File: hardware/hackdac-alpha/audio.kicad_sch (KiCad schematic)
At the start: 30 parts, among them J3 I2C, J4 AUDIO OUT, P2 P22, Q4 2N7002, Q5 2N7002, U8 MCP1700T-3302E/MB, U9 PCM5102

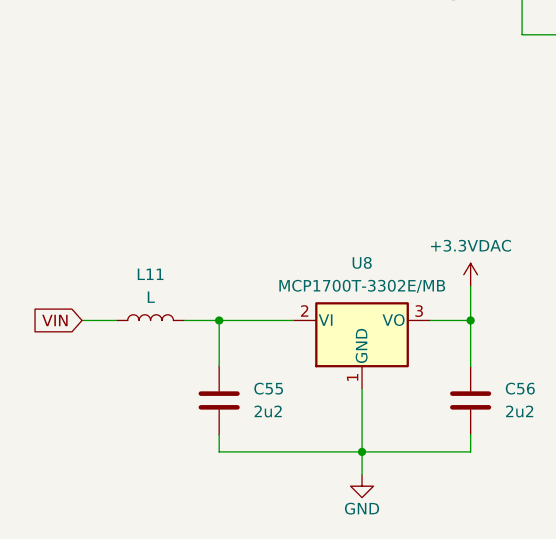
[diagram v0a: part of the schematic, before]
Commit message: Add missing component values
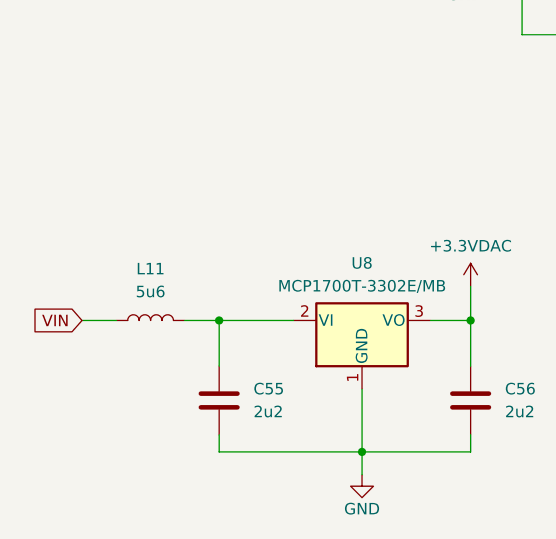
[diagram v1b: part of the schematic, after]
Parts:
- L11: value L -> 5u6
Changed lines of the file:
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@@
 		(fields_autoplaced yes)
 		(property "Reference" "L11"
-			(at 48.895 151.765 90)
+			(at 48.895 151.13 90)
 			(effects
 				(font
@@
 			)
 		)
-		(property "Value" "L"
-			(at 48.895 154.305 90)
+		(property "Value" "5u6"
+			(at 48.895 153.67 90)
 			(effects
 				(font

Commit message: Update with V2 mods
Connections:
- net TCXO_CLK: now reaches P2.2 (Pin_2)
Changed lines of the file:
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@@
+	(wire
+		(pts
+			(xy 76.2 29.845) (xy 80.01 29.845)
+		)
+		(stroke
+			(width 0)
+			(type default)
+		)
+	)
 	(wire
 		(pts
@@
 				(hide yes)
 			)
+		)
+	)
+	(global_label "TCXO_CLK"
+		(shape input)
+		(at 80.01 29.845 0)
+		(fields_autoplaced yes)
+		(effects
+			(font
+				(size 1.27 1.27)
+			)
+			(justify left)
+		)
+		(property "Intersheetrefs" "${INTERSHEET_REFS}"
+			(at 92.3085 29.845 0)
+			(effects
+				(font
+					(size 1.27 1.27)
+				)
+				(justify left)
+				(hide yes)
+			)

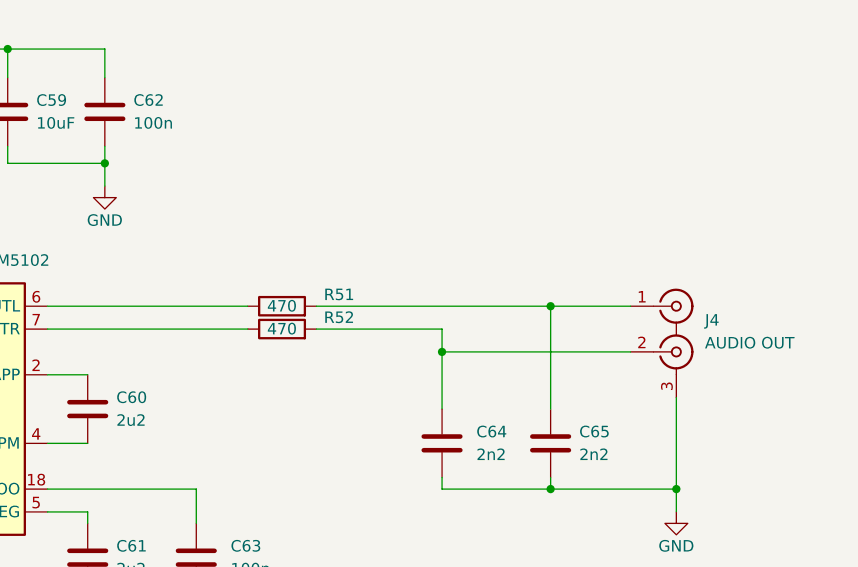
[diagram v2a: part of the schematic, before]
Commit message: Final values for V2 board
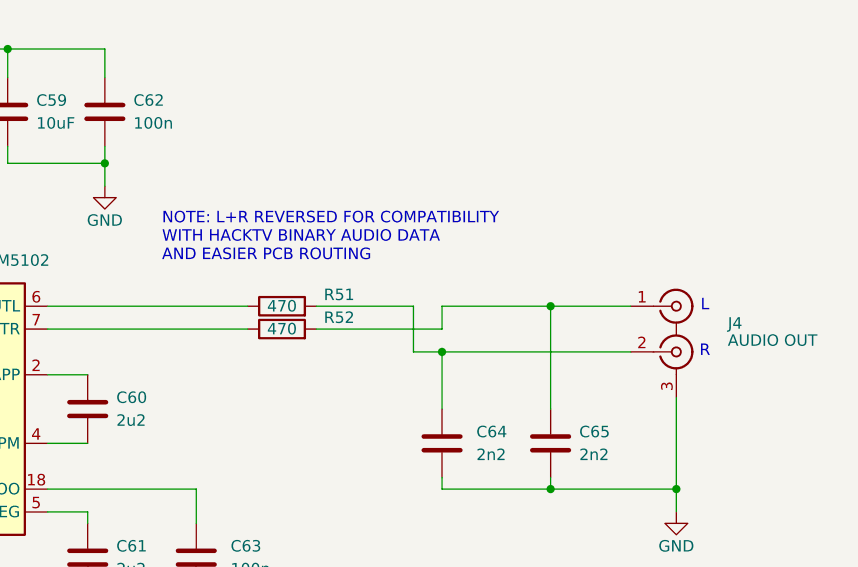
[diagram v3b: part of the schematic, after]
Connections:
- net at C64.1, J4.2 (IN2): now also R51.2; no longer R52.2
- net at C65.1, J4.1 (IN1): now also R52.2; no longer R51.2
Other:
- note added: "L"
- note added: "NOTE: L+R REVERSED FOR COMPATIBILITY WITH HACKTV BINARY AUDIO DATA AND EASIER PCB ROUTING"
- note added: "R"
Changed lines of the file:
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@@
 	)
 	(junction
+		(at 224.79 114.935)
+		(diameter 0)
+		(color 0 0 0 0)
+	)
+	(junction
 		(at 236.855 109.855)
 		(diameter 0)
@@
 		(color 0 0 0 0)
 	)
-	(junction
-		(at 224.79 114.935)
-		(diameter 0)
-		(color 0 0 0 0)
-	)
 	(wire
 		(pts
@@
 	(wire
 		(pts
+			(xy 221.615 114.935) (xy 224.79 114.935)
+		)
+		(stroke
+			(width 0)
+			(type default)
+		)
+	)
+	(wire
+		(pts
+			(xy 221.615 109.855) (xy 221.615 114.935)
+		)
+		(stroke
+			(width 0)
+			(type default)
+		)
+	)
+	(wire
+		(pts
 			(xy 185.42 141.605) (xy 185.42 142.875)
 		)
@@
 	(wire
 		(pts
+			(xy 210.82 109.855) (xy 221.615 109.855)
+		)
+		(stroke
+			(width 0)
+			(type default)
+		)
+	)
+	(wire
+		(pts
 			(xy 153.67 117.475) (xy 155.575 117.475)
 		)
@@
 	(wire
 		(pts
+			(xy 224.79 109.855) (xy 236.855 109.855)
+		)
+		(stroke
+			(width 0)
+			(type default)
+		)
+	)
+	(wire
+		(pts
 			(xy 147.955 127.635) (xy 155.575 127.635)
 		)
@@
 	(wire
 		(pts
-			(xy 197.485 130.175) (xy 197.485 133.985)
+			(xy 224.79 112.395) (xy 224.79 109.855)
 		)
 		(stroke
@@
 	(wire
 		(pts
-			(xy 84.455 156.845) (xy 84.455 161.925)
+			(xy 197.485 130.175) (xy 197.485 133.985)
 		)
 		(stroke
@@
 	(wire
 		(pts
-			(xy 176.53 81.28) (xy 176.53 84.455)
+			(xy 84.455 156.845) (xy 84.455 161.925)
 		)
 		(stroke
@@
 	(wire
 		(pts
-			(xy 210.82 112.395) (xy 224.79 112.395)
+			(xy 176.53 81.28) (xy 176.53 84.455)
 		)
 		(stroke
@@
 	(wire
 		(pts
-			(xy 139.7 117.475) (xy 144.145 117.475)
+			(xy 210.82 112.395) (xy 224.79 112.395)
 		)
 		(stroke
@@
 	(wire
 		(pts
-			(xy 224.79 130.175) (xy 224.79 128.905)
+			(xy 139.7 117.475) (xy 144.145 117.475)
 		)
 		(stroke
@@
 	(wire
 		(pts
-			(xy 130.175 49.53) (xy 130.175 34.29)
+			(xy 224.79 130.175) (xy 224.79 128.905)
 		)
 		(stroke
@@
 	(wire
 		(pts
-			(xy 168.275 137.795) (xy 168.275 140.335)
+			(xy 130.175 49.53) (xy 130.175 34.29)
 		)
 		(stroke
@@
 	(wire
 		(pts
-			(xy 224.79 112.395) (xy 224.79 114.935)
+			(xy 168.275 137.795) (xy 168.275 140.335)
 		)
 		(stroke
@@
 	(wire
 		(pts
-			(xy 210.82 109.855) (xy 236.855 109.855)
-		)
-		(stroke
-			(width 0)
-			(type default)
-		)
-	)
-	(wire
-		(pts
 			(xy 180.975 117.475) (xy 185.42 117.475)
 		)
@@
 		)
 	)
+	(text "NOTE: L+R REVERSED FOR COMPATIBILITY\nWITH HACKTV BINARY AUDIO DATA\nAND EASIER PCB ROUTING"
+		(exclude_from_sim no)
+		(at 193.675 102.235 0)
+		(effects
+			(font
+				(size 1.27 1.27)
+			)
+			(justify left)
+		)
+	)
+	(text "R"
+		(exclude_from_sim no)
+		(at 254 114.935 0)
+		(effects
+			(font
+				(size 1.27 1.27)
+			)
+		)
+	)
+	(text "L"
+		(exclude_from_sim no)
+		(at 254 109.855 0)
+		(effects
+			(font
+				(size 1.27 1.27)
+			)
+		)
+	)
 	(label "I2S_WS"
 		(at 50.165 47.625 0)
@@
 		(on_board yes)
 		(dnp no)
-		(fields_autoplaced yes)
 		(property "Reference" "J4"
-			(at 254 111.4182 0)
+			(at 256.54 111.76 0)
 			(effects
 				(font
@@
 		)
 		(property "Value" "AUDIO OUT"
-			(at 254 113.9582 0)
+			(at 256.54 113.665 0)
 			(effects
 				(font

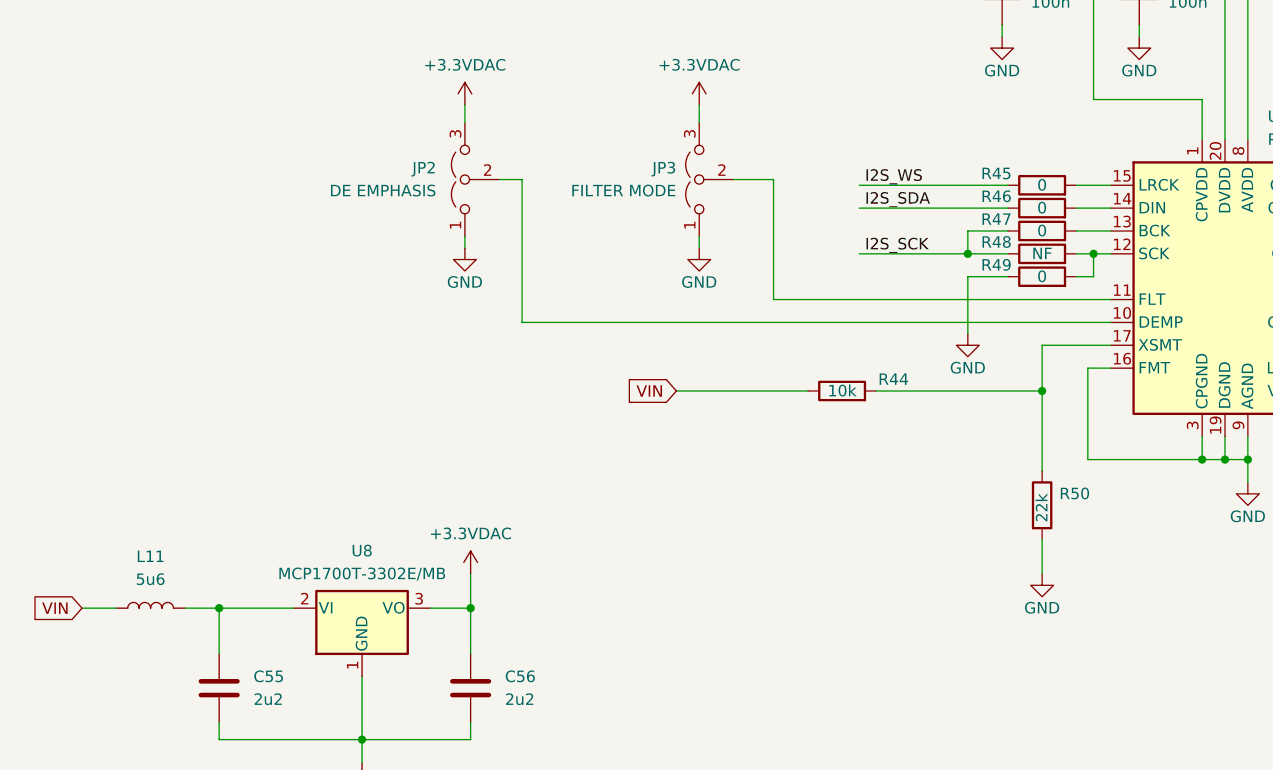
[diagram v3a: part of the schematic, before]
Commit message: More V3 component rationalisation
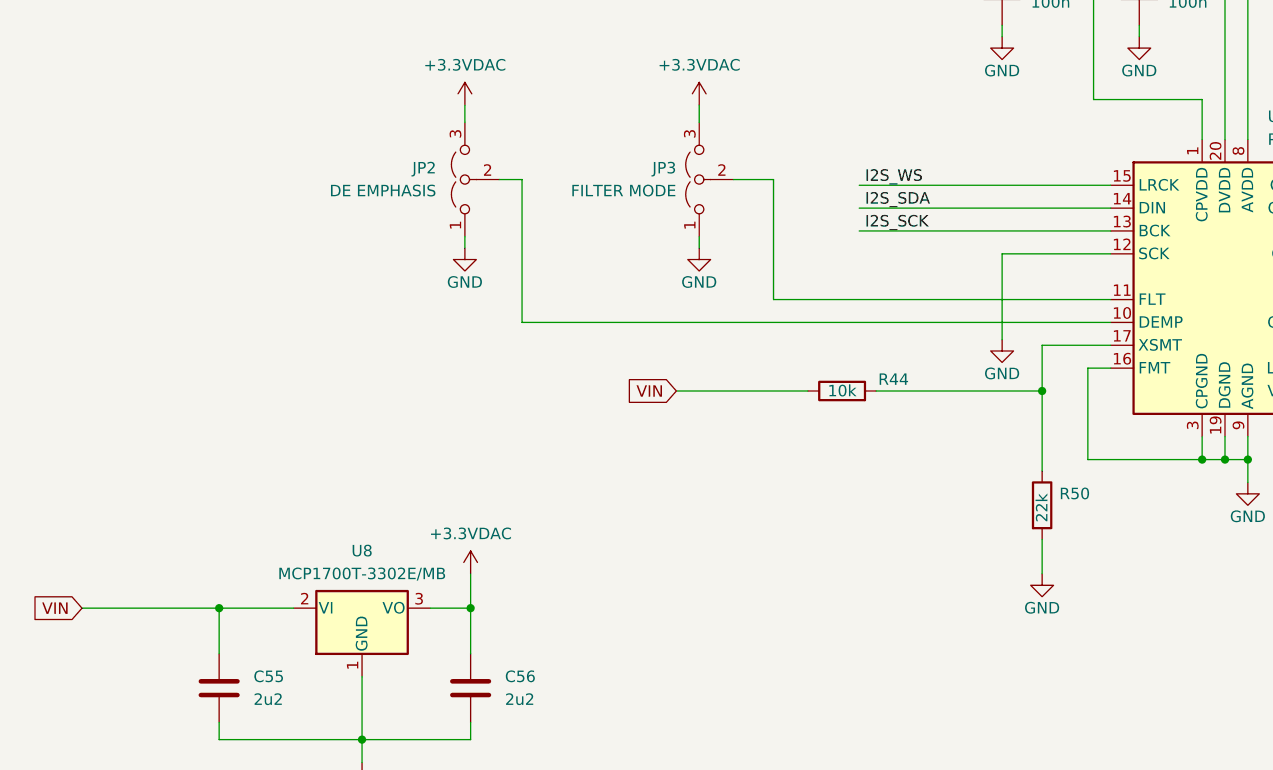
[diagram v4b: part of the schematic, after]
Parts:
- removed L11: 5u6, Inductor_SMD:L_1210_3225Metric, symbol Device:L
- removed R45, R46, R47, R49: 0, Resistor_SMD:R_0603_1608Metric, symbol Device:R
- removed R48: NF, Resistor_SMD:R_0603_1608Metric, symbol Device:R
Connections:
- net GND: now also U9.12 (SCK)
- net I2S_SCK: now also U9.13 (BCK)
- net I2S_SDA: now also U9.14 (DIN)
- net I2S_WS: now also U9.15 (LRCK)
- net VIN: now also C55.1, U8.2 (VI)

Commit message: Last of major V3 changes
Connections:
- net PWR_EN: now reaches P2.22 (Pin_22)
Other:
- note added: "NO FIT"
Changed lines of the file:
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@@
+	(wire
+		(pts
+			(xy 76.2 55.245) (xy 81.915 55.245)
+		)
+		(stroke
+			(width 0)
+			(type default)
+		)
+	)
 	(wire
 		(pts
@@
 	(wire
 		(pts
-			(xy 97.155 57.785) (xy 97.155 49.53)
+			(xy 98.425 57.785) (xy 98.425 49.53)
 		)
 		(stroke
@@
 	(wire
 		(pts
-			(xy 76.2 57.785) (xy 97.155 57.785)
+			(xy 76.2 57.785) (xy 98.425 57.785)
 		)
 		(stroke
@@
 	(wire
 		(pts
-			(xy 97.155 49.53) (xy 100.33 49.53)
+			(xy 98.425 49.53) (xy 100.33 49.53)
 		)
 		(stroke
@@
 	(text "NOTE: L+R REVERSED FOR COMPATIBILITY\nWITH HACKTV BINARY AUDIO DATA\nAND EASIER PCB ROUTING"
 		(exclude_from_sim no)
-		(at 193.675 102.235 0)
+		(at 204.47 102.235 0)
 		(effects
 			(font
@@
 			)
 			(justify left)
+		)
+	)
+	(text "NO FIT"
+		(exclude_from_sim no)
+		(at 147.32 38.1 0)
+		(effects
+			(font
+				(size 1.27 1.27)
+			)
 		)
 	)
@@
 	)
 	(label "SCL"
-		(at 82.55 60.325 0)
+		(at 93.345 60.325 0)
 		(fields_autoplaced yes)
 		(effects
@@
 	)
 	(label "SDA"
-		(at 82.55 57.785 0)
+		(at 93.345 57.785 0)
 		(fields_autoplaced yes)
 		(effects
@@
 			(effects
 				(font
+					(size 1.27 1.27)
+				)
+				(justify left)
+				(hide yes)
+			)
+		)
+	)
+	(global_label "PWR_EN"
+		(shape input)
+		(at 81.915 55.245 0)
+		(fields_autoplaced yes)
+		(effects
+			(font
+				(size 1.27 1.27)
+			)
+			(justify left)
+		)
+		(property "Intersheetrefs" "${INTERSHEET_REFS}"
+			(at 92.3387 55.245 0)
+			(effects
+				(font

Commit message: V3 PCB WIP
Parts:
- renumbered C55 to C54, C56 to C55, C57 to C56, C58 to C57, C59 to C58, C60 to C59, C61 to C60, C62 to C61, C63 to C62, C64 to C63, C65 to C64, J3 to J4, J4 to J5, Q4 to Q5, Q5 to Q6, R50 to R45, R51 to R46, R52 to R47

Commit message: V3 layout mostly complete
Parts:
- JP2, JP3: footprint Jumper:SolderJumper-3_P1.3mm_Open_Pad1.0x1.5mm -> Jumper:SolderJumper-3_P1.3mm_Bridged12_Pad1.0x1.5mm
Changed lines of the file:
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@@
 			)
 		)
-		(property "Footprint" "Jumper:SolderJumper-3_P1.3mm_Open_Pad1.0x1.5mm"
+		(property "Footprint" "Jumper:SolderJumper-3_P1.3mm_Bridged12_Pad1.0x1.5mm"
 			(at 83.82 109.22 0)
 			(effects
@@
 			)
 		)
-		(property "Footprint" "Jumper:SolderJumper-3_P1.3mm_Open_Pad1.0x1.5mm"
+		(property "Footprint" "Jumper:SolderJumper-3_P1.3mm_Bridged12_Pad1.0x1.5mm"
 			(at 109.855 109.22 0)
 			(effects

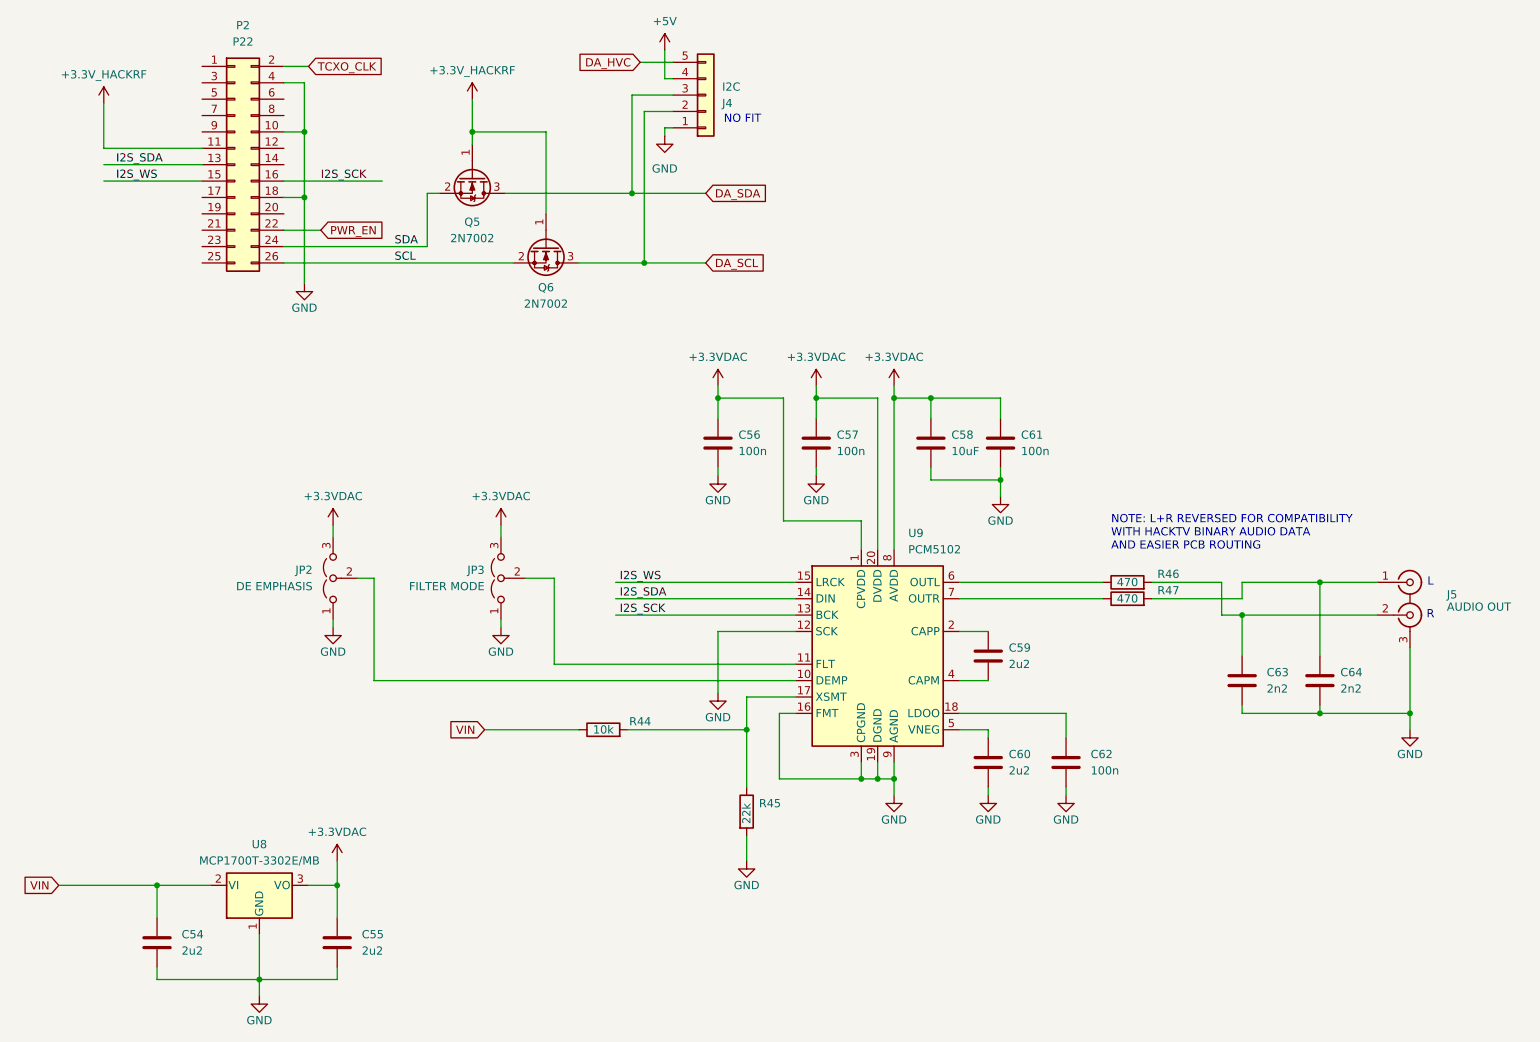
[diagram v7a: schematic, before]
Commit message: Optional caps for DAC supply
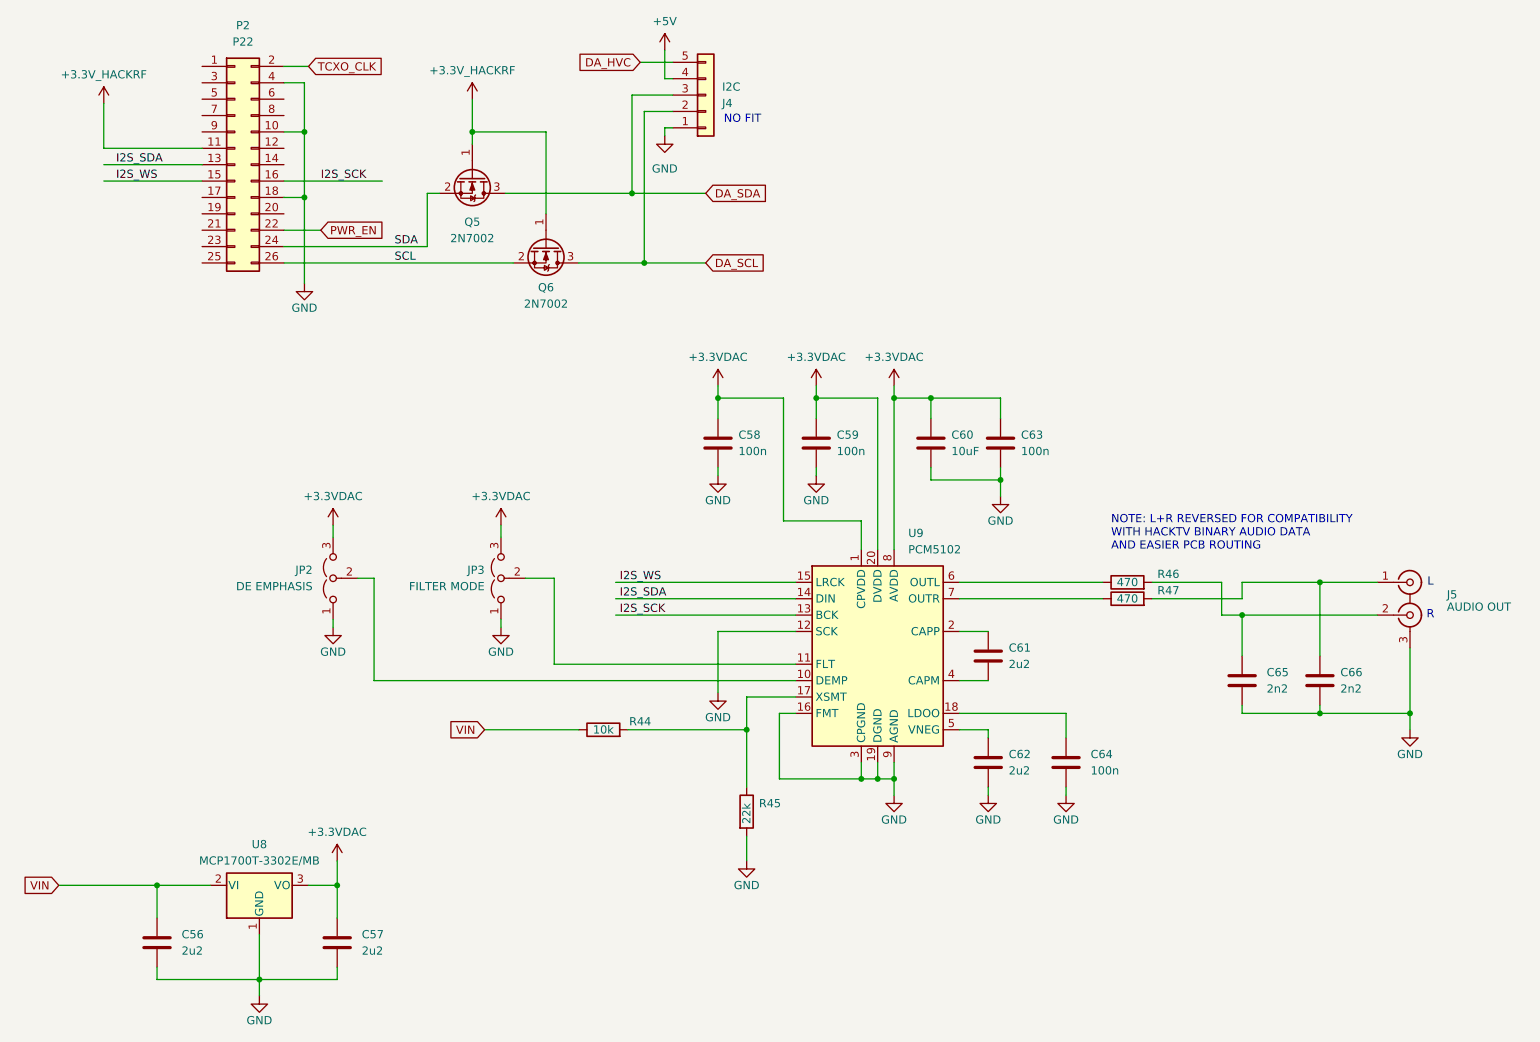
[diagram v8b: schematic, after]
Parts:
- renumbered C54 to C56, C55 to C57, C56 to C58, C57 to C59, C58 to C60, C59 to C61, C60 to C62, C61 to C63, C62 to C64, C63 to C65, C64 to C66
